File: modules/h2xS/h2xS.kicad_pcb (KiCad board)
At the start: 2 copper layers, 84 x 40.7 mm, 55 parts, among them J1 2, J10 11, J1001 Conn_01x04_Male, J1002 Conn_01x12_Male, J1003 Conn_01x04_Male, J1004 Conn_01x12_Male, J1005 Conn_01x12_Male, J1006 Conn_01x06_Male, J1007 Barrel_Jack_MountingPin, J11 12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

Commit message: h2x with Sensor Shield in work
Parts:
- removed the H1 at (109.5, 102.8)
- removed the H2 at (142.5, 102.8)
- removed the H3 at (109.5, 69.8)
- removed the H4 at (142.5, 69.8)
- removed J1001, J1003: Conn_01x04_Male, Connector_PinHeader_2.54mm:PinHeader_1x04_P2.54mm_Vertical
- removed J1002, J1004, J1005: Conn_01x12_Male, Connector_PinHeader_2.54mm:PinHeader_1x12_P2.54mm_Vertical
- removed J1006: Conn_01x06_Male, Connector_PinHeader_2.54mm:PinHeader_1x06_P2.54mm_Vertical
- removed J1007: Barrel_Jack_MountingPin, Connector_BarrelJack:BarrelJack_Horizontal
- removed JO1: 2, Connector_PinHeader_2.54mm:PinHeader_1x01_P2.54mm_Vertical
- removed JO10: 11, Connector_PinHeader_2.54mm:PinHeader_1x01_P2.54mm_Vertical
- removed JO11: 12, Connector_PinHeader_2.54mm:PinHeader_1x01_P2.54mm_Vertical
- removed JO12: 13, Connector_PinHeader_2.54mm:PinHeader_1x01_P2.54mm_Vertical
- removed JO13: A0, Connector_PinHeader_2.54mm:PinHeader_1x01_P2.54mm_Vertical
- removed JO14: A1, Connector_PinHeader_2.54mm:PinHeader_1x01_P2.54mm_Vertical
- removed JO15: A2, Connector_PinHeader_2.54mm:PinHeader_1x01_P2.54mm_Vertical
- removed JO16: A3, Connector_PinHeader_2.54mm:PinHeader_1x01_P2.54mm_Vertical
- removed JO17: A4, Connector_PinHeader_2.54mm:PinHeader_1x01_P2.54mm_Vertical
- removed JO18: A5, Connector_PinHeader_2.54mm:PinHeader_1x01_P2.54mm_Vertical
- removed JO19: Vcc, Connector_PinHeader_2.54mm:PinHeader_1x01_P2.54mm_Vertical
- removed JO2: 3, Connector_PinHeader_2.54mm:PinHeader_1x01_P2.54mm_Vertical
- removed JO20: Gnd, Connector_PinHeader_2.54mm:PinHeader_1x01_P2.54mm_Vertical
- removed JO3: 4, Connector_PinHeader_2.54mm:PinHeader_1x01_P2.54mm_Vertical
- removed JO4: 5, Connector_PinHeader_2.54mm:PinHeader_1x01_P2.54mm_Vertical
- removed JO5: 6, Connector_PinHeader_2.54mm:PinHeader_1x01_P2.54mm_Vertical
- removed JO6: 7, Connector_PinHeader_2.54mm:PinHeader_1x01_P2.54mm_Vertical
- removed JO7: 8, Connector_PinHeader_2.54mm:PinHeader_1x01_P2.54mm_Vertical
- removed JO8: 9, Connector_PinHeader_2.54mm:PinHeader_1x01_P2.54mm_Vertical
- removed JO9: 10, Connector_PinHeader_2.54mm:PinHeader_1x01_P2.54mm_Vertical
- added H5: MountingHole, MountingHole:MountingHole_3.2mm_M3, F.Cu at (143.5, 54.6)
- added H6: MountingHole, MountingHole:MountingHole_3.2mm_M3, F.Cu at (110.5, 54.6)
- added H7: MountingHole, MountingHole:MountingHole_3.2mm_M3, F.Cu at (143.5, 87.6)
- added H8: MountingHole, MountingHole:MountingHole_3.2mm_M3, F.Cu at (110.5, 87.6)
- added J21: Conn_01x10_Male, Connector_PinSocket_2.54mm:PinSocket_1x10_P2.54mm_Vertical, F.Cu at (138.4, 54.6)
- added J22: Conn_01x12_Male, Connector_PinHeader_2.54mm:PinHeader_1x12_P2.54mm_Vertical, F.Cu at (151.1, 53.3)
- added J23: Conn_01x12_Male, Connector_PinHeader_2.54mm:PinHeader_1x12_P2.54mm_Vertical, F.Cu at (153.7, 81.3)
- added J24: Conn_01x04_Male, Connector_PinHeader_2.54mm:PinHeader_1x04_P2.54mm_Vertical, F.Cu at (148.6, 86.4)
- added J25: Conn_01x04_Male, Connector_PinHeader_2.54mm:PinHeader_1x04_P2.54mm_Vertical, F.Cu at (148.6, 88.9)
- added J26: Conn_01x12_Male, Connector_PinHeader_2.54mm:PinHeader_1x12_P2.54mm_Vertical, F.Cu at (156.2, 81.3)
- added J27: Conn_01x10_Male, Connector_PinSocket_2.54mm:PinSocket_1x10_P2.54mm_Vertical, F.Cu at (115.6, 87.6)
- added J28: Conn_01x06_Male, Connector_PinHeader_2.54mm:PinHeader_1x06_P2.54mm_Vertical, F.Cu at (123.2, 90.2)
- added J29: Barrel_Jack_Switch, Connector_BarrelJack:BarrelJack_Horizontal, F.Cu at (77.5, 71.1)
- moved H1 15.3 mm to (67.3, 87.6)
- moved H2 15.3 mm to (100.3, 87.6)
- moved J11 15.3 mm to (74.9, 87.6)
- moved J12 15.3 mm to (77.5, 87.6)
- moved J13 15.3 mm to (80.0, 87.6)
- moved J14 15.3 mm to (82.5, 87.6)
- moved J15 15.3 mm to (85.1, 87.6)
- moved J16 15.3 mm to (87.6, 87.6)
- moved J17 15.3 mm to (90.2, 87.6)
- moved J18 15.3 mm to (92.7, 87.6)
- moved J19 15.3 mm to (72.4, 87.6)
- moved J20 15.3 mm to (95.2, 87.6)
- moved H3 15.3 mm to (67.3, 54.6)
- moved H4 15.3 mm to (100.3, 54.6)
- moved J1 15.3 mm to (95.2, 54.6)
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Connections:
- J19 pad 1: Net-(J19-Pad1) -> VCC
- J20 pad 1: Net-(J20-Pad1) -> GND
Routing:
- net GND: track 0.00 -> 46.7 mm, vias 0 -> 1
- net VCC: track 0.00 -> 35.6 mm
- net Net-(J19-Pad1): track 30.5 -> 0.00 mm, vias 1 -> 0
- net Net-(J11-Pad1): track 27.9 -> 0.00 mm, vias 1 -> 0
- net Net-(J12-Pad1): track 25.4 -> 0.00 mm, vias 1 -> 0
- net Net-(J21-Pad4): track 22.9 -> 0.00 mm, vias 1 -> 0
- net Net-(J21-Pad5): track 20.3 -> 0.00 mm, vias 1 -> 0
- net Net-(J13-Pad1): track 22.9 -> 2.54 mm, vias 1 -> 0
- net Net-(J21-Pad6): track 17.8 -> 0.00 mm, vias 1 -> 0
- net Net-(J14-Pad1): track 20.3 -> 2.54 mm, vias 1 -> 0
- net Net-(J21-Pad7): track 15.2 -> 0.00 mm, vias 1 -> 0
- net Net-(J15-Pad1): track 17.8 -> 2.54 mm, vias 1 -> 0
- net Net-(J17-Pad1): track 12.7 -> 26.1 mm
- net Net-(J21-Pad8): track 12.7 -> 0.00 mm, vias 1 -> 0
- net Net-(J16-Pad1): track 15.2 -> 2.54 mm, vias 1 -> 0
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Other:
- board size 84 x 40.7 mm -> 95.2 x 40.6 mm

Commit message: Sensor Shield ready
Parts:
- moved J29 2.54 mm to (77.5, 68.6)
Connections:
- net Net-(J1-Pad1) renamed /2
- net Net-(J10-Pad1) renamed /11
- net Net-(J11-Pad1) renamed /12
- net Net-(J12-Pad1) renamed /13
- net Net-(J13-Pad1) renamed /A0
- net Net-(J14-Pad1) renamed /A1
- net Net-(J15-Pad1) renamed /A2
- net Net-(J16-Pad1) renamed /A3
- net Net-(J17-Pad1) renamed /A4
- net Net-(J18-Pad1) renamed /A5
- net Net-(J2-Pad1) renamed /3
- net Net-(J21-Pad3) renamed /4
- net Net-(J21-Pad4) renamed /5
- net Net-(J21-Pad5) renamed /6
- net Net-(J21-Pad6) renamed /7
- net Net-(J21-Pad7) renamed /8
- net Net-(J21-Pad8) renamed /9
- net Net-(J21-Pad9) renamed /10
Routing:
- net VCC: track 35.6 -> 151.8 mm, vias 0 -> 1
- net GND: track 46.7 -> 156.8 mm, vias 1 -> 2
- net /11: track 0.00 -> 97.3 mm
- net /10: track 0.00 -> 95.9 mm, vias 0 -> 1
- net /9: track 0.00 -> 94.1 mm, vias 0 -> 1
- net /8: track 0.00 -> 92.2 mm, vias 0 -> 1
- net /7: track 0.00 -> 90.3 mm, vias 0 -> 1
- net /12: track 0.00 -> 88.8 mm, vias 0 -> 2
- net /6: track 0.00 -> 88.4 mm, vias 0 -> 1
- net /13: track 0.00 -> 88.3 mm, vias 0 -> 2
- net /5: track 0.00 -> 88.2 mm, vias 0 -> 1
- net /2: track 18.6 -> 87.2 mm, vias 0 -> 1
- net /A5: track 21.2 -> 89.2 mm
- net /3: track 19.2 -> 87.1 mm, vias 0 -> 1
- net /A4: track 26.1 -> 93.4 mm
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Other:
- board text added: "+5V"
- board text added: "D10"
- board text added: "D11"
- board text added: "D12"
- board text added: "D13"
- board text added: "D2"
- board text added: "D3"
- board text added: "D4"
- board text added: "D5"
- board text added: "D6"
- board text added: "D7"
- board text added: "D8"
- board text added: "D9"
- board text added: "I2C"
- board text added: "Power"
- board text added: "SCL"
- board text added: "SDA"

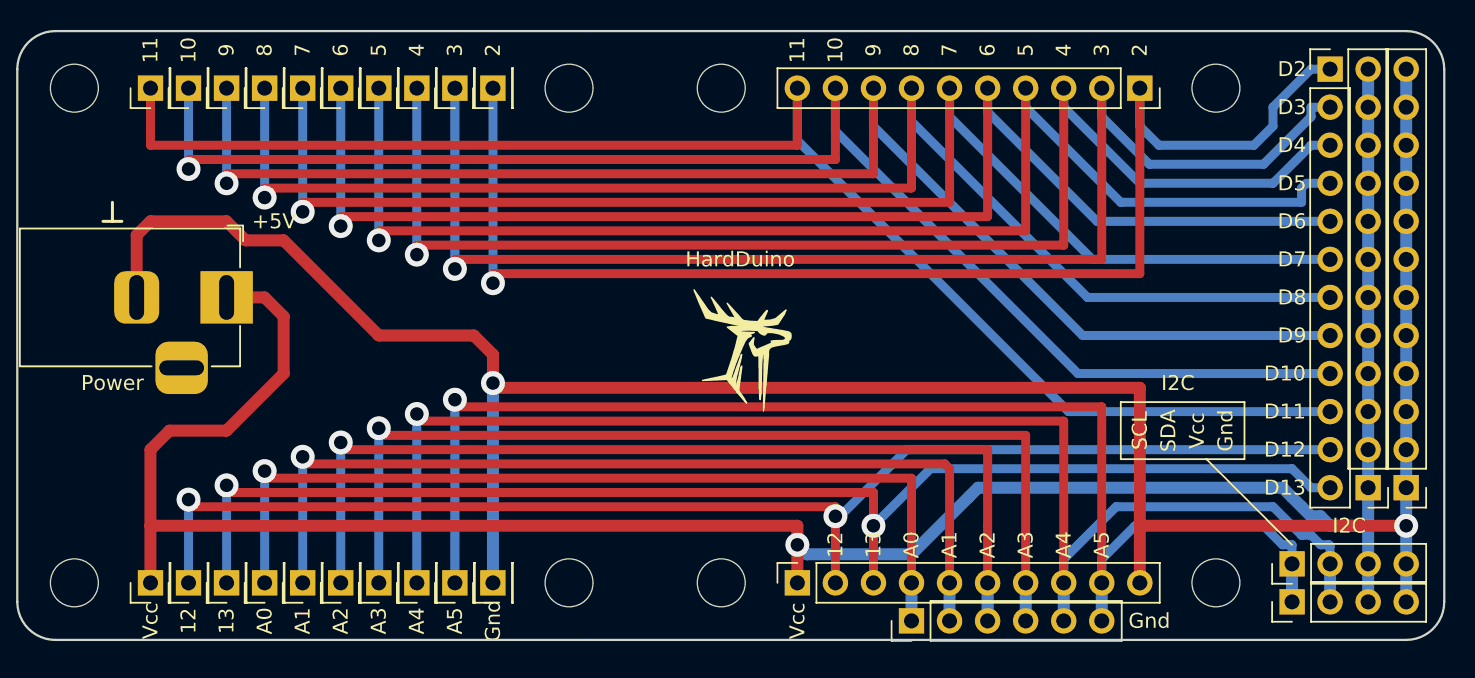
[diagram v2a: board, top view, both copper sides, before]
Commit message: Enlarge pads. Add photomask.
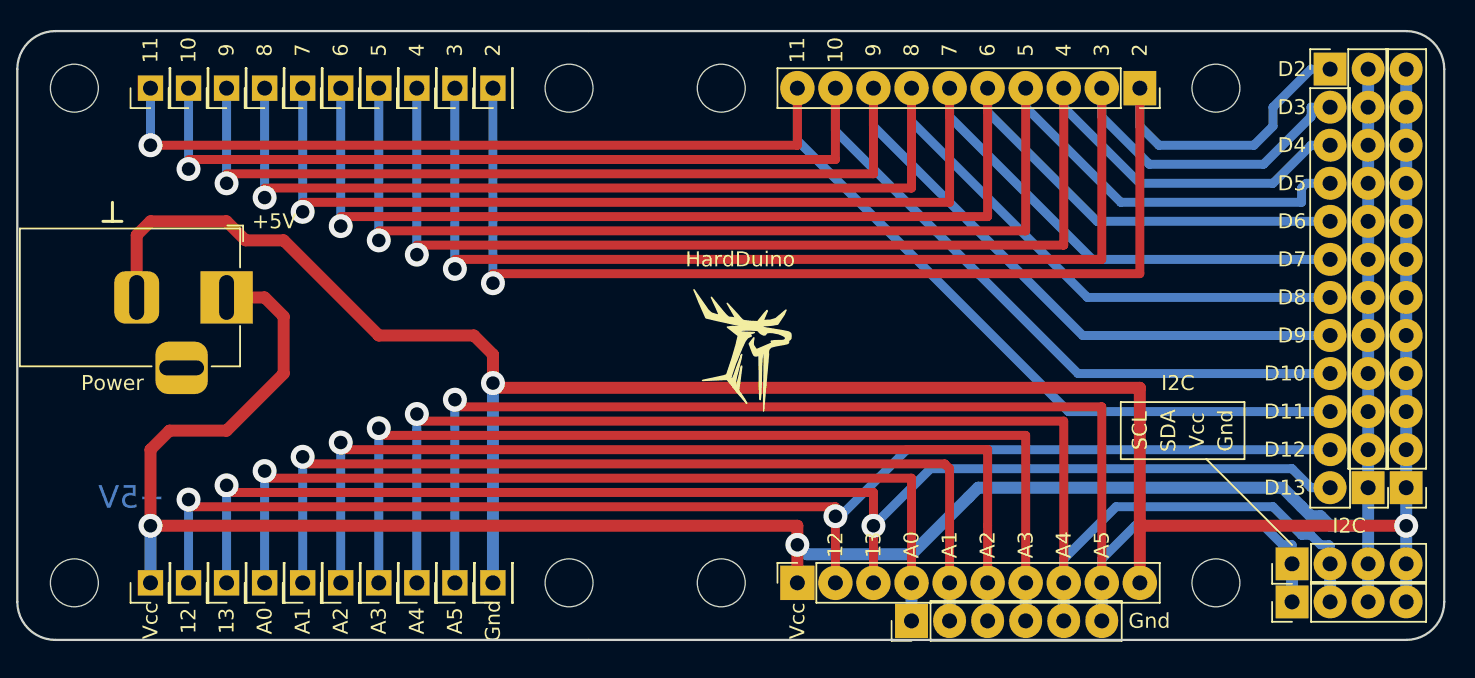
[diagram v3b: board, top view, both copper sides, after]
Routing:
- net VCC: vias 1 -> 2
- net /11: vias 0 -> 1

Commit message: Another side
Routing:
- net GND: track 156.8 -> 154.0 mm
- net VCC: track 151.8 -> 153.5 mm
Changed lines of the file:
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@@
   )
   (setup
-    (last_trace_width 0.25)
+    (last_trace_width 1)
     (user_trace_width 0.6)
     (user_trace_width 0.8)
@@
     )
   )
-  (gr_text +5V (at 71.12 81.915) (layer B.Cu)
+  (gr_text +5V (at 68.58 81.915) (layer B.Cu)
     (effects (font (size 1.5 1.5) (thickness 0.3)) (justify mirror))
   )
@@
   (segment (start 115.57 83.82) (end 115.57 87.63) (width 0.8) (layer F.Cu) (net 1))
   (segment (start 72.39 87.63) (end 72.39 83.82) (width 0.8) (layer B.Cu) (net 1))
-  (segment (start 80.01 68.58) (end 77.47 68.58) (width 0.8) (layer F.Cu) (net 1))
-  (segment (start 72.39 78.74) (end 73.66 77.47) (width 0.8) (layer F.Cu) (net 1))
-  (segment (start 72.39 83.82) (end 72.39 78.74) (width 0.8) (layer F.Cu) (net 1))
-  (segment (start 73.66 77.47) (end 77.47 77.47) (width 0.8) (layer F.Cu) (net 1))
-  (segment (start 77.47 77.47) (end 81.28 73.66) (width 0.8) (layer F.Cu) (net 1))
-  (segment (start 81.28 73.66) (end 81.28 69.85) (width 0.8) (layer F.Cu) (net 1))
-  (segment (start 81.28 69.85) (end 80.01 68.58) (width 0.8) (layer F.Cu) (net 1))
   (segment (start 153.67 83.82) (end 151.13 83.82) (width 0.8) (layer B.Cu) (net 1))
   (segment (start 153.67 83.82) (end 153.67 81.28) (width 0.8) (layer B.Cu) (net 1))
@@
   (segment (start 72.39 83.82) (end 115.57 83.82) (width 0.8) (layer F.Cu) (net 1))
   (via (at 72.39 83.82) (size 1.6) (drill 0.9) (layers F.Cu B.Cu) (net 1))
+  (segment (start 72.39 83.82) (end 72.39 78.74) (width 1) (layer B.Cu) (net 1))
+  (segment (start 72.39 78.74) (end 73.66 77.47) (width 1) (layer B.Cu) (net 1))
+  (segment (start 73.66 77.47) (end 78.74 77.47) (width 1) (layer B.Cu) (net 1))
+  (segment (start 78.74 77.47) (end 81.915 74.295) (width 1) (layer B.Cu) (net 1))
+  (segment (start 81.915 74.295) (end 81.915 69.85) (width 1) (layer B.Cu) (net 1))
+  (segment (start 81.915 69.85) (end 80.645 68.58) (width 1) (layer B.Cu) (net 1))
+  (segment (start 80.645 68.58) (end 77.47 68.58) (width 1) (layer B.Cu) (net 1))
   (via (at 95.25 74.295) (size 1.6) (drill 0.9) (layers F.Cu B.Cu) (net 2))
   (segment (start 95.25 74.6125) (end 138.43 74.6125) (width 0.8) (layer F.Cu) (net 2))
@@
   (via (at 156.21 83.82) (size 1.6) (drill 0.9) (layers F.Cu B.Cu) (net 2))
   (segment (start 95.25 87.63) (end 95.25 74.295) (width 0.8) (layer B.Cu) (net 2))
-  (segment (start 71.47 68.58) (end 71.47 64.42) (width 0.8) (layer F.Cu) (net 2))
-  (segment (start 71.47 64.42) (end 72.39 63.5) (width 0.8) (layer F.Cu) (net 2))
-  (segment (start 72.39 63.5) (end 77.47 63.5) (width 0.8) (layer F.Cu) (net 2))
-  (segment (start 77.47 63.5) (end 78.74 64.77) (width 0.8) (layer F.Cu) (net 2))
-  (segment (start 78.74 64.77) (end 81.28 64.77) (width 0.8) (layer F.Cu) (net 2))
-  (segment (start 81.28 64.77) (end 87.63 71.12) (width 0.8) (layer F.Cu) (net 2))
-  (segment (start 95.25 72.39) (end 93.98 71.12) (width 0.8) (layer F.Cu) (net 2))
-  (segment (start 95.25 72.39) (end 95.25 74.295) (width 0.8) (layer F.Cu) (net 2))
-  (segment (start 87.63 71.12) (end 93.98 71.12) (width 0.8) (layer F.Cu) (net 2))
+  (segment (start 92.075 71.12) (end 95.25 74.295) (width 1) (layer B.Cu) (net 2))
+  (segment (start 71.47 68.58) (end 71.47 66.325) (width 1) (layer B.Cu) (net 2))
+  (segment (start 71.47 66.325) (end 73.66 64.135) (width 1) (layer B.Cu) (net 2))
+  (segment (start 73.66 64.135) (end 80.01 64.135) (width 1) (layer B.Cu) (net 2))
+  (segment (start 80.01 64.135) (end 81.28 65.405) (width 1) (layer B.Cu) (net 2))
+  (segment (start 81.28 65.405) (end 82.55 65.405) (width 1) (layer B.Cu) (net 2))
+  (segment (start 82.55 65.405) (end 87.63 70.485) (width 1) (layer B.Cu) (net 2))
+  (segment (start 91.44 70.485) (end 92.075 71.12) (width 1) (layer B.Cu) (net 2))
+  (segment (start 87.63 70.485) (end 91.44 70.485) (width 1) (layer B.Cu) (net 2))
   (via (at 95.25 67.6275) (size 1.6) (drill 0.9) (layers F.Cu B.Cu) (net 4))
   (segment (start 95.25 66.9925) (end 138.43 66.9925) (width 0.6) (layer F.Cu) (net 4))
